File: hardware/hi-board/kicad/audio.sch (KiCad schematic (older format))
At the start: 10 parts, among them J2 Speaker, U1 LM386

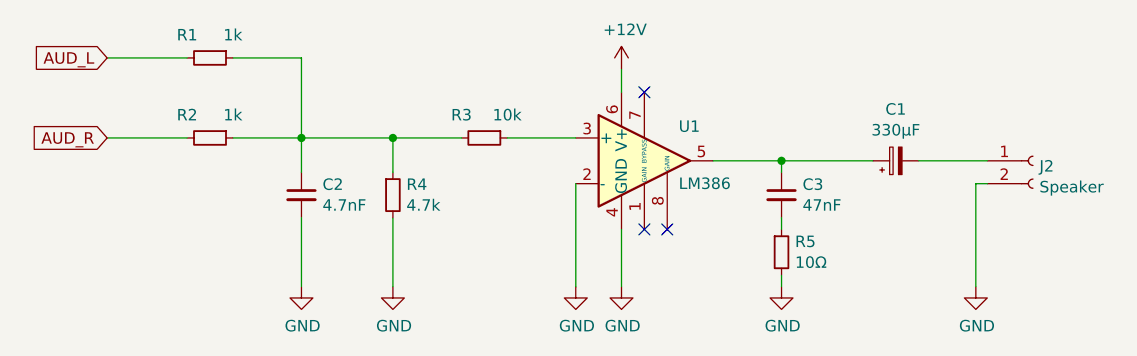
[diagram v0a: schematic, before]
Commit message: Add display and power supply to schematics
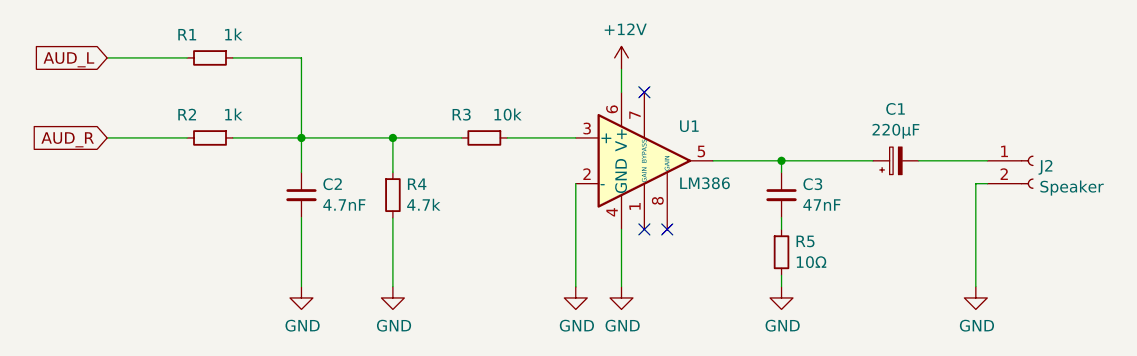
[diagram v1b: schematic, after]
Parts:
- C1: value 330µF -> 220µF; footprint (none) -> Capacitor_THT:CP_Radial_D6.3mm_P2.50mm
- J2: footprint (none) -> Connector_PinHeader_2.54mm:PinHeader_1x02_P2.54mm_Vertical
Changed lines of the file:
@@
 $Descr A4 11693 8268
 encoding utf-8
-Sheet 3 3
+Sheet 3 5
 Title "Audio"
 Date ""
@@
 P 6500 3500
 F 0 "C1" V 6725 3500 50  0000 C CNN
-F 1 "330µF" V 6634 3500 50  0000 C CNN
-F 2 "" H 6500 3500 50  0001 C CNN
+F 1 "220µF" V 6634 3500 50  0000 C CNN
+F 2 "Capacitor_THT:CP_Radial_D6.3mm_P2.50mm" H 6500 3500 50  0001 C CNN
 F 3 "~" H 6500 3500 50  0001 C CNN
 	1    6500 3500
@@
 F 0 "J2" H 7128 3476 50  0000 L CNN
 F 1 "Speaker" H 7128 3385 50  0000 L CNN
-F 2 "" H 7100 3500 50  0001 C CNN
+F 2 "Connector_PinHeader_2.54mm:PinHeader_1x02_P2.54mm_Vertical" H 7100 3500 50  0001 C CNN
 F 3 "~" H 7100 3500 50  0001 C CNN
 	1    7100 3500
